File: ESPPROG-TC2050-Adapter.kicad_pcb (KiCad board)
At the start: 2 copper layers, 20.8 x 24.1 mm, 6 parts, among them J1 DebugHeader_Cortex-M_JTAG_10p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, J2 CONN ESP-PROG, J3 2x3 Card Edge Progamming Conn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, U1 GT-USB-7010ASV

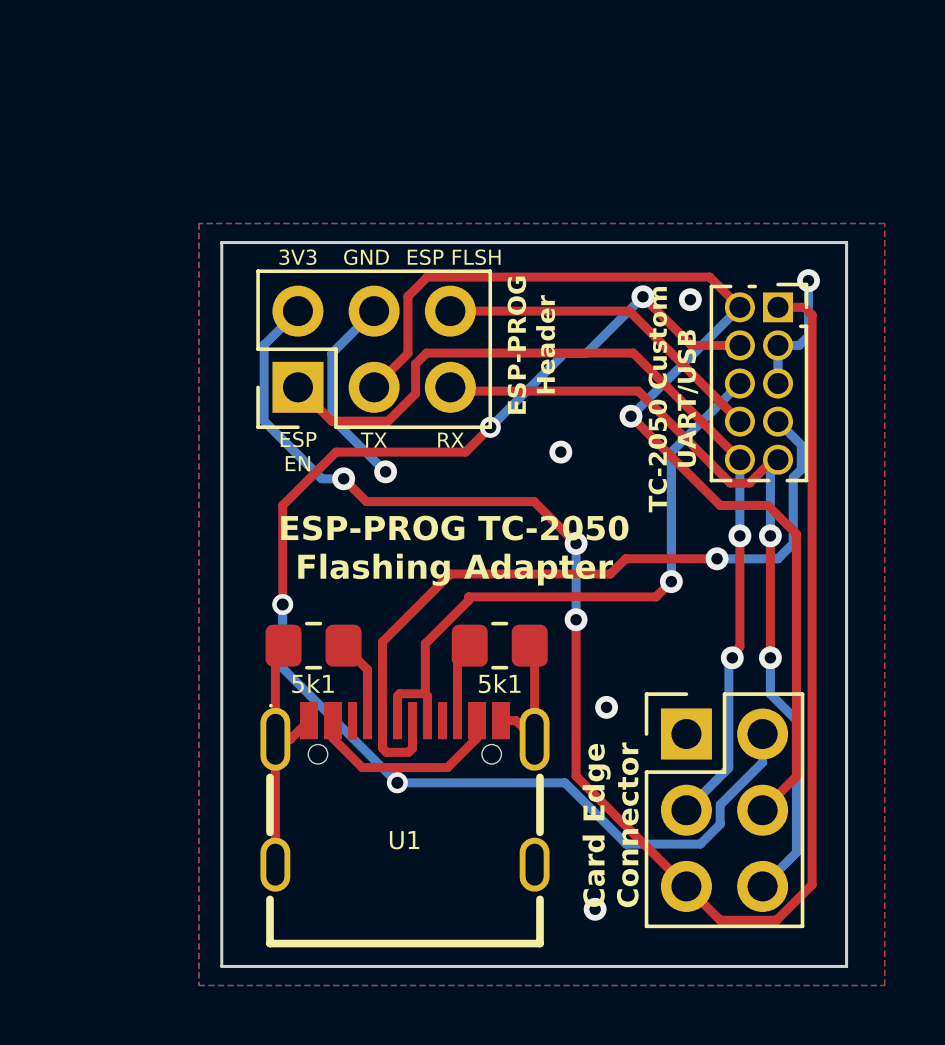
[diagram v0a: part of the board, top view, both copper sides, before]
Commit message: Majority of v1.1 changes
* Removed card-edge connector
* Added SOICbite 2x4P 2.54mm header with ESP8266 pinout
* changed TC-2050 pinout to more default UART one
* changed board dimensions to better fit on top of ESP-PROG
* added to-scale picture of ESP-PROG in background to get better feel
  for alignment
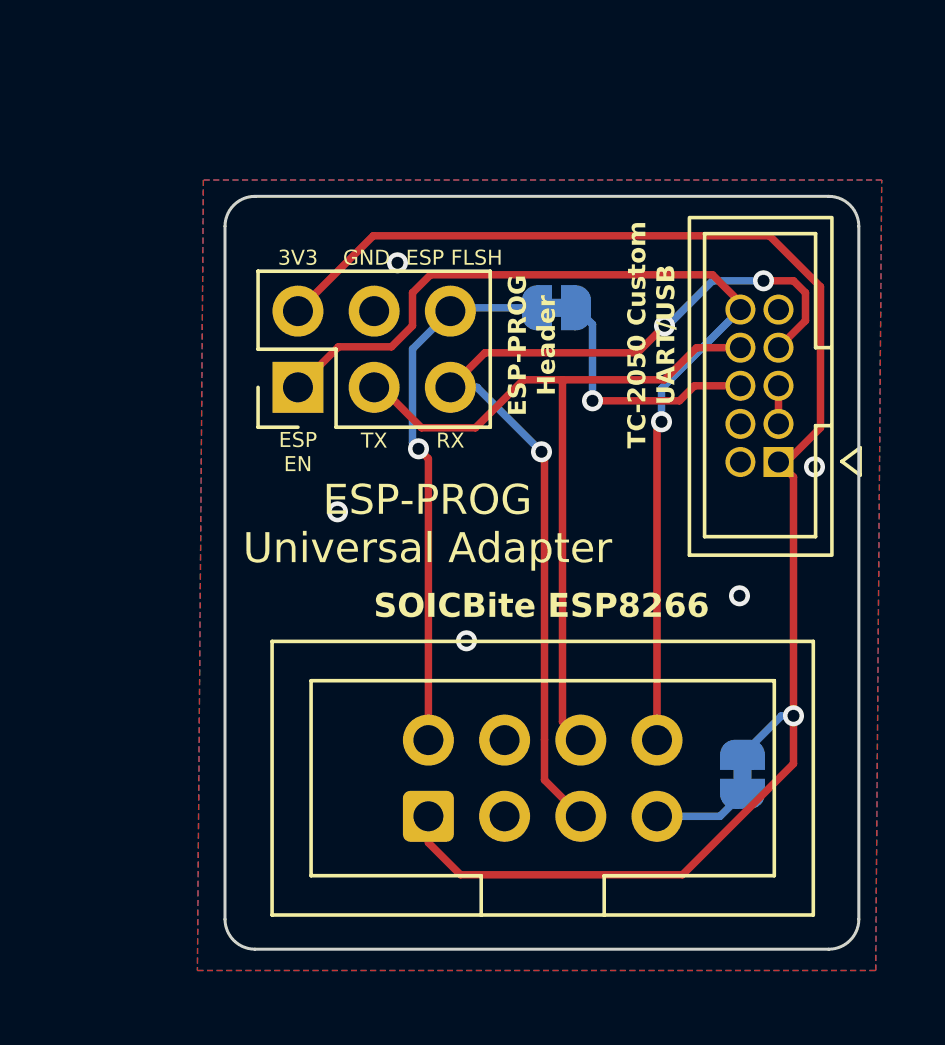
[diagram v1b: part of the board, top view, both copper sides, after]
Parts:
- removed J1: DebugHeader_Cortex-M_JTAG_10p_TagConnect, Connector_PinSocket_1.27mm:PinSocket_2x05_P1.27mm_Vertical
- removed J3: 2x3 Card Edge Progamming Connector, Connector_PinHeader_2.54mm:PinHeader_2x03_P2.54mm_Vertical
- removed R1, R2: 5k1, Resistor_SMD:R_0805_2012Metric_Pad1.20x1.40mm_HandSolder
- removed U1: GT-USB-7010ASV, jmux-footprints:USB-C-SMD_G-SWITCH_GT-USB-7010ASV
- added J4: ProgConn-SOICBite, Connector_IDC:IDC-Header_2x04_P2.54mm_Vertical, F.Cu at (139.7, 79.5)
- added J5: DebugHeader_Cortex-M_SWD_UART_10p_TagConnect, jmux-footprints:TC-2050-IDC-SOCKET, F.Cu at (148.7, 58.5)
- added JP1: CH_PD EN, Jumper:SolderJumper-2_P1.3mm_Bridged_RoundedPad1.0x1.5mm, B.Cu at (150.2, 78.0)
- added JP2: SolderJumper_2_Bridged, Jumper:SolderJumper-2_P1.3mm_Bridged_RoundedPad1.0x1.5mm, B.Cu at (144.0, 62.5)
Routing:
- net /5V_VUSB: track 52.8 -> 0.00 mm, vias 4 -> 0
- net /USB_D-: track 25.1 -> 0.00 mm, vias 1 -> 0
- net Earth: track 24.3 -> 1.27 mm, vias 6 -> 5
- net /USB_D+: track 21.1 -> 0.00 mm, vias 1 -> 0
- net /ESP_TXD0: track 36.8 -> 26.1 mm, vias 1 -> 0
- net /SWO_IO0: track 0.00 -> 8.46 mm, vias 0 -> 1
- net /ESP_IO0: track 10.8 -> 18.6 mm, vias 0 -> 1
- net /ESP_RXD0: track 27.8 -> 32.5 mm, vias 2 -> 3
- net /CH_PD: track 0.00 -> 3.16 mm
- net Net-(U1-CC1): track 2.83 -> 0.00 mm
- net Net-(U1-CC2): track 2.67 -> 0.00 mm
- net /ESP_EN: track 30.7 -> 33.1 mm, vias 2 -> 1
- net /VDD_U: track 54.6 -> 53.3 mm, vias 3 -> 1
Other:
- board size 20.8 x 24.1 mm -> 21.1 x 25.1 mm
- board text added: "0xjmux v1.1 11-2023"
- board text added: "CH_PD"
- board text added: "CH_PD EN"
- board text added: "EN"
- board text added: "ESP-PROG Universal Adapter"
- board text added: "IO0"
- board text added: "IO0-SWO"
- board text added: "SOICBite ESP8266"
- board text added: "VDD"
- board text removed: "0xjmux v1.0 11-2023"
- board text removed: "5V"
- board text removed: "Card Edge Connector"
- board text removed: "ESP BT"
- board text removed: "ESP-PROG TC-2050 Flashing Adapter"
- board text removed: "USB D+"
- board text removed: "USB D-"
- board text removed: "USB-OTG Compatible ESPs Only"

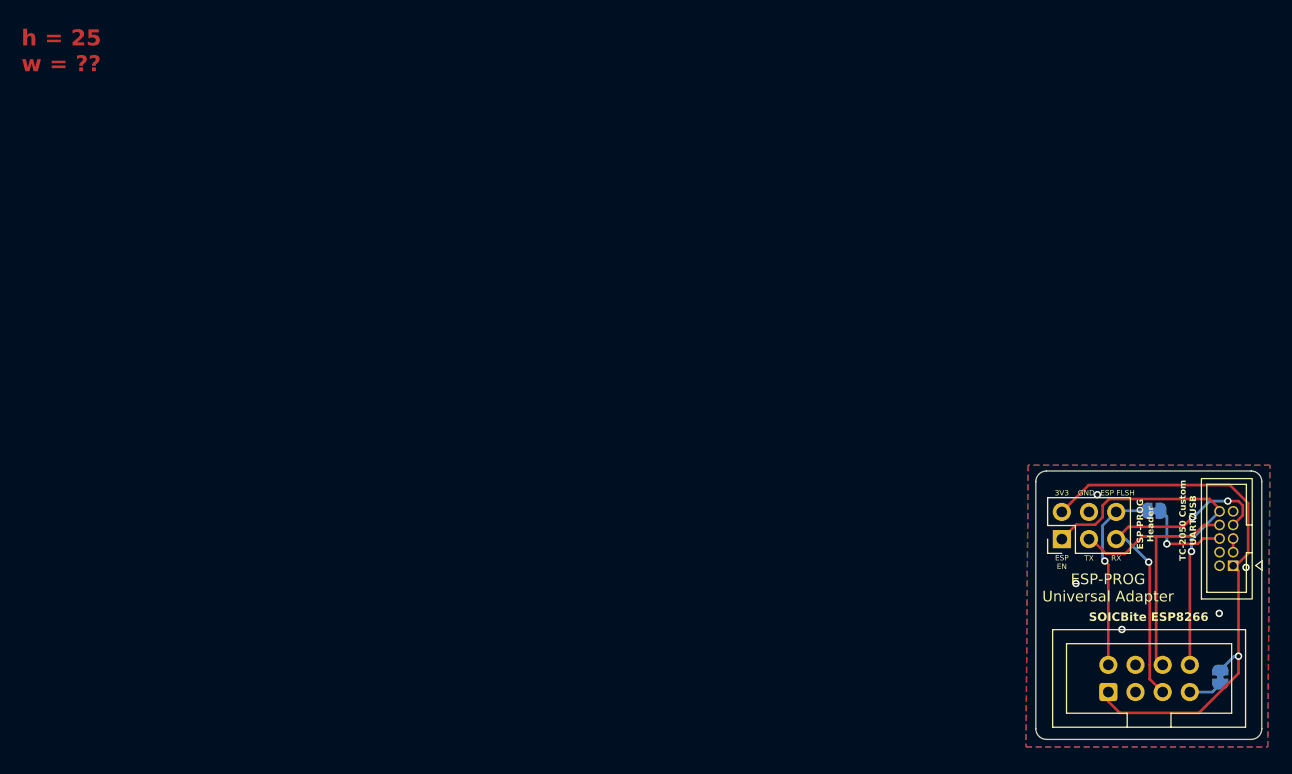
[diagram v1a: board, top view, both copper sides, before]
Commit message: Redesign for v1.2
* Added second F header to connect to ESP-PROG's JTAG header
* added connectors for TC2050 and SOICbite for JTAG
* had to extend board length as a result
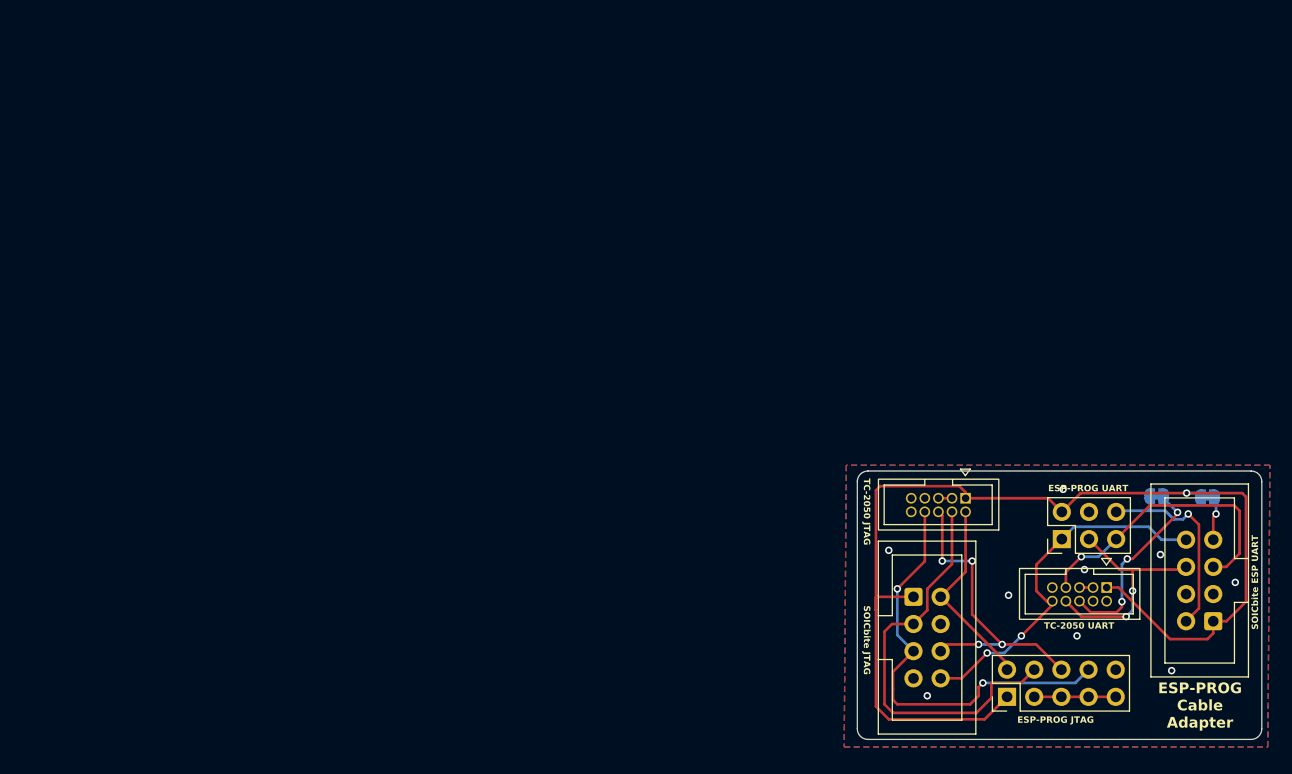
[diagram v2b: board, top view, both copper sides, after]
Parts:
- added J1: Conn_02x05_Odd_Even, Connector_PinSocket_2.54mm:PinSocket_2x05_P2.54mm_Vertical, B.Cu at (130.3, 79.9)
- added J3: DebugHeader_Cortex-M_JTAG_10p_TagConnect, jmux-footprints:TC-2050-IDC-SOCKET, F.Cu at (117.3, 64.0)
- added J6: SOICbite-JTAG, Connector_IDC:IDC-Header_2x04_P2.54mm_Vertical, F.Cu at (121.5, 70.5)
- moved J5 22.9 mm to (130.5, 72.3), turned to -90 degrees
- moved JP1 16.8 mm to (149.0, 61.2), turned to 180 degrees
- moved J4 11.8 mm to (149.5, 72.8), turned to 180 degrees
- moved JP2 1.37 mm to (144.2, 61.1)
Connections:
- net /ESP_IO0 renamed /ESP_BOOT
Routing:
- net /VDD_U: track 53.3 -> 103.9 mm
- net /ESP_TDI: track 0.00 -> 40.3 mm, vias 0 -> 2
- net /ESP_TCK: track 0.00 -> 38.6 mm
- net /ESP_TDO: track 0.00 -> 29.0 mm, vias 0 -> 4
- net /ESP_TMS: track 0.00 -> 18.3 mm
- net /SWO_IO0: track 8.46 -> 17.9 mm, vias 1 -> 3
- net Earth: track 1.27 -> 10.2 mm, vias 5 -> 9
- net /ESP_RXD0: track 32.5 -> 27.4 mm, vias 3 -> 1
- net /ESP_TXD0: track 26.1 -> 21.3 mm, vias 0 -> 2
- net /ESP_BOOT: track 18.6 -> 19.6 mm
- net /CH_PD: track 3.16 -> 4.13 mm, vias 0 -> 1
- net /ESP_EN: track 33.1 -> 34.0 mm, vias 1 -> 2
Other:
- board size 21.1 x 25.1 mm -> 37.8 x 25.1 mm
- board text added: "0xjmux v1.2 11-2023"
- board text added: "BOOT"
- board text added: "EN/RST"
- board text added: "ESP-PROG Cable Adapter"
- board text added: "ESP-PROG JTAG"
- board text added: "ESP-PROG UART"
- board text added: "SOICbite ESP UART"
- board text added: "SOICbite JTAG"
- board text added: "TC-2050 JTAG"
- board text added: "TC-2050 UART"
- board text added: "TCK"
- board text added: "TDI"
- board text added: "TDO"
- board text added: "TMS"
- board text added: "jacobbokor.com"
- board text added: "nRST"
- board text added: "x"
- board text removed: "0xjmux v1.1 11-2023"
- board text removed: "3V3"
- board text removed: "ESP EN"
- board text removed: "ESP FLSH"
- board text removed: "ESP-PROG Header"
- board text removed: "ESP-PROG Universal Adapter"
- board text removed: "IO0"
- board text removed: "SOICBite ESP8266"
- board text removed: "TC-2050 Custom UART/USB"
- board text removed: "h = 25 w = ??"
